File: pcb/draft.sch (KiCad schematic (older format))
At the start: 0 parts

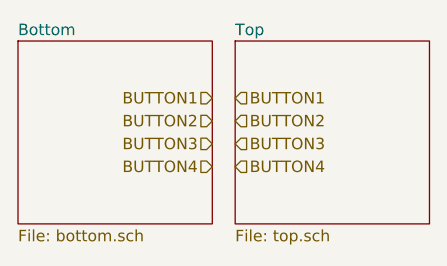
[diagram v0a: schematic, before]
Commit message: Add buzzer and clean up
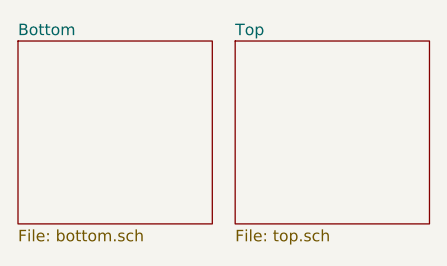
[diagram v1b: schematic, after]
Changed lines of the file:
@@
 Comment4 ""
 $EndDescr
-Text HLabel 5550 3300 0    50   Input ~ 0
-BUTTON1
-Text HLabel 5650 3500 2    50   Input ~ 0
-BUTTON3
 $Sheet
 S 4700 3050 850  800
@@
 F1 "top.sch" 50
 $EndSheet
-Text HLabel 5550 3400 0    50   Input ~ 0
-BUTTON2
-Text HLabel 5650 3300 2    50   Input ~ 0
-BUTTON1
-Text HLabel 5650 3400 2    50   Input ~ 0
-BUTTON2
-Text HLabel 5650 3600 2    50   Input ~ 0
-BUTTON4
-Text HLabel 5550 3500 0    50   Input ~ 0
-BUTTON3
-Text HLabel 5550 3600 0    50   Input ~ 0
-BUTTON4
 $EndSCHEMATC
